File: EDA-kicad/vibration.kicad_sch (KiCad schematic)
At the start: 4 parts

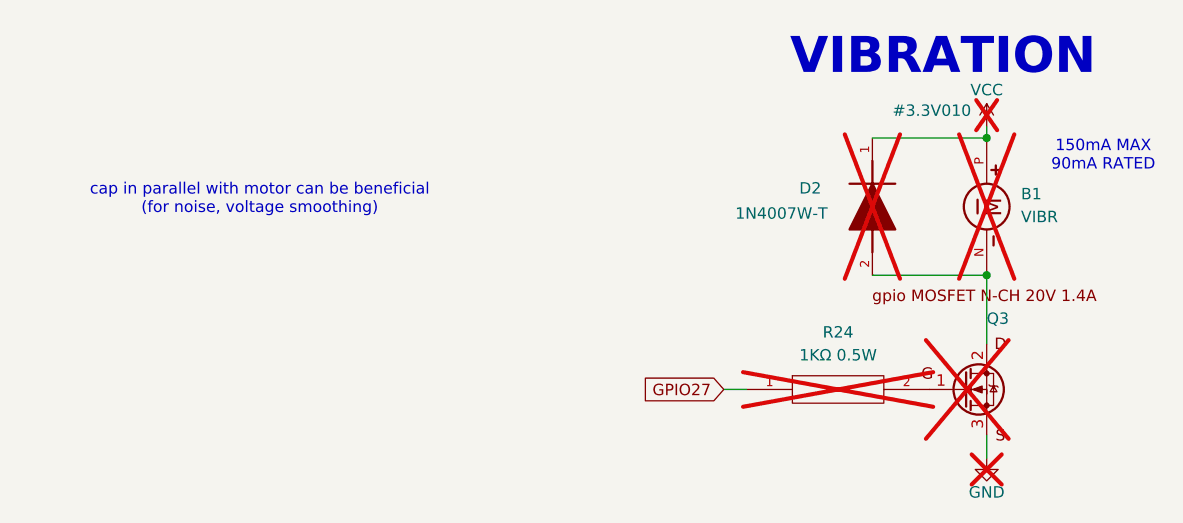
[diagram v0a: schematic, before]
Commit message: reannotate entire schematic
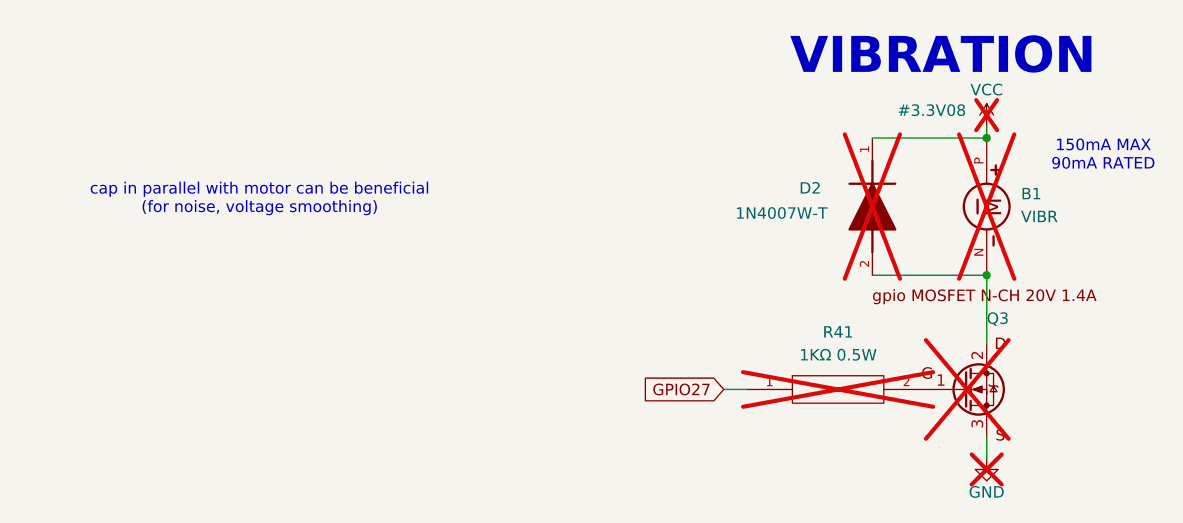
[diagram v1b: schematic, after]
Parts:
- renumbered R24 to R41
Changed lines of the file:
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@@
 			"AAAAAAAAAAAAAAAAAAAAAAAAAAAAAAAAAAAAAAAAAAAAAAAAAAAAAAAAAAAAAAAAAAAAAAAAAAAA"
 			"AAAAAAAAAAAAAAAAAAAAAAAAAAAAAAAAAAAAAAAAAAAAAAAAAAAAAAAAAAAAAAAAAAAAAAAAAAAA"
-			"AAAAAAAAAAAAAAAAAAAAAAAAAAAAAAAAAAAAAAAAAAAAAAAAAAAAAAAAAAAAAAAAAA=="
+			"AAAAAAAAAAAAAAAAAAAAAAAAAAAAAAAAAAAAAAAAAAAAAAAAAAAAAAAAAAAAAAAAAEFBQUFBQUFB"
+			"QUFBQUFBQUFBQUFBQUFBQUFBQUFBQUFBQUFBQUFBQUFBQUFBQUFBQUFBQUFBQUFBQUFBQUFBQUFB"
+			"QUFBQUFBQUFBQUFBQUFBQUFBQUFBQUFBQUFBQUFBQUFBQUFBQUFBQUFBQUFBQUFBQUFBQUFBQUFB"
+			"QUFBQUFBQUFBQUFBQUFBQUFBQUFBQUFBQUFBQUFBQUFBQUFBQUFBQUFBQUFBQUFBQUFBQUFBQUFB"
+			"QUFBQUFBQUFBQUFBQUFBQUFBQUFBQUFBQUFBQUFBQUFBQUFBQUFBQUFBQUFBQUFBQUFBQUFBQUFB"
+			"QUFBQUFBQUFBQUFBQUFBQUFBQUFBQUFBQUFBQUFBQUFBQUFBQUFBQUFBQUFBQUFBQUFBQUFBQUFB"
+			"QUFBQUFBQUFBQUFBQUFBQUFBQUFBQUFBQUFBQUFBQUFBQUFBQUFBQUFBQUFBQUFBQUFBQUFBQUFB"
+			"QUFBQUFBQUFBQUFBQUFBQUFBQUFBQUFBQUFBQUFBQUFBQUFBQUFBQUFBQUFBQUFBQUFBQUFBQUFB"
+			"QUFBQUFBQUFBQUFBQUFBQUFBQUFBQUFBQUFBQUFBQUFBQUFBQUFBQUFBQUFBQUFBQUFBQUFBQUFB"
+			"QUFBQUFBQUFBQUFBQUFBQUFBQUFBQUFBQUFBQUFBQUFBQUFBQUFBQUFBQUFBQUFBQUFBQUFBQUFB"
+			"QUFBQUFBQUFBQUFBQUFBQUFBQUFBQUFBQUFBQUFBQUFBQUFBQUFBQUFBQUFBQUFBQUFBQUFBQUFB"
+			"QUFBQUFBQUFBQUFBQUFBQUFBQUFBQUFBQUFBQUFBQUFBQUFBQUFBQUFBQUFBQUFBQUFBQUFBQUFB"
+			"QUFBQUFBQUFBQUFBQUFBQUFBQUFBQUFBQUFBQUFBQUFBQUFBQUFBQUFBQUFBQUFBQUFBQUFBQUFB"
+			"QUFBQUFBQUFBQUFBQUFBQUFBQUFBQUFBQUFBQUFBQUFBQUFBQUFBQUFBQUFBQUFBQUFBQUFBQUFB"
+			"QUFBQUFBQUFBQUFBQUFBQUFBQUFBQUFBQUFBQUFBQUFBQUFBQUFBQUFBQUFBQUFBQUFBQUFBQUFB"
+			"QUFBQUFBQUFBQUFBQUFBQUFBQUFBQUFBQUFBQUFBQUFBQUFBQUFBQUFBQUFBQUFBQUFBQUFBQUFB"
+			"QUFBQUFBQUFBQUFBQUFBQUFBQUFBQUFBQUFBQUFBQUFBQUFBQUFBQUFBQUFBQUFBQUFBQUFBQUFB"
+			"QUFBQUFBQUFBQUFBQUFBQUFBQUFBQUFBQUFBQUFBQUFBQUFBQUFBQUFBQUFBQUFBQUFBQUFBQUFB"
+			"QUFBQUFBQUFBQUFBQUFBQUFBQUFBQUFBQUFBQUFBQUFBQUFBQUFBQUFBQUFBQdBdAQ=="
 		)
 	)
@@
 		(on_board yes)
 		(dnp yes)
-		(property "Reference" "#PWR0129"
+		(property "Reference" "#PWR0147"
 			(at 176.53 124.46 0)
 			(effects
@@
 			(project "cm5-carrier"
 				(path "/28c5e4fe-1ec7-4477-97f0-d2ec1401fad5/b44a98f4-0347-4633-8437-b3dfeaa625db"
-					(reference "#PWR0129")
+					(reference "#PWR0147")
 					(unit 1)
 				)
@@
 		(dnp yes)
 		(fields_autoplaced yes)
-		(property "Reference" "R24"
+		(property "Reference" "R41"
 			(at 160.02 104.14 0)
 			(effects
@@
 			(project "cm5-carrier"
 				(path "/28c5e4fe-1ec7-4477-97f0-d2ec1401fad5/b44a98f4-0347-4633-8437-b3dfeaa625db"
-					(reference "R24")
+					(reference "R41")
 					(unit 1)
 				)
@@
 		(on_board yes)
 		(dnp yes)
-		(property "Reference" "#3.3V010"
+		(property "Reference" "#3.3V08"
 			(at 170.434 79.502 0)
 			(effects
@@
 			(project "cm5-carrier"
 				(path "/28c5e4fe-1ec7-4477-97f0-d2ec1401fad5/b44a98f4-0347-4633-8437-b3dfeaa625db"
-					(reference "#3.3V010")
+					(reference "#3.3V08")
 					(unit 1)
 				)
